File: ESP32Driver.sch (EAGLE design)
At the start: 90 parts, among them IC1 ESP-WROOM-32_VIA, IC3 FT231XQ, SW2 434111025826, T1.1 BC847A, T1.2 BC847A, T1.3 BC847A, T1.4 BC847A, X1 USB

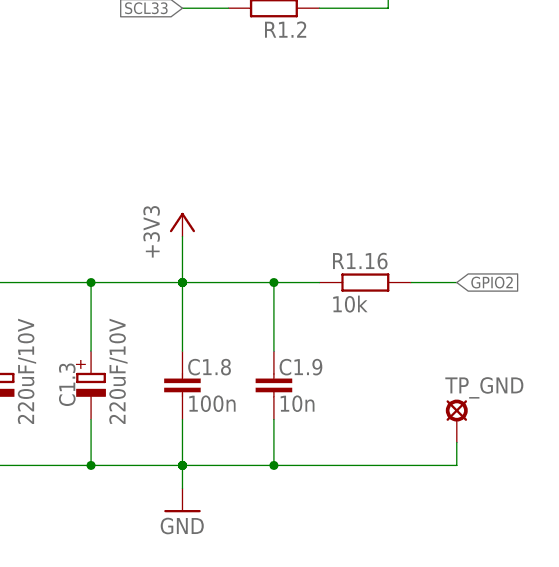
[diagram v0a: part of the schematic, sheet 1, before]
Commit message: delete GPIO2 pullup resistor
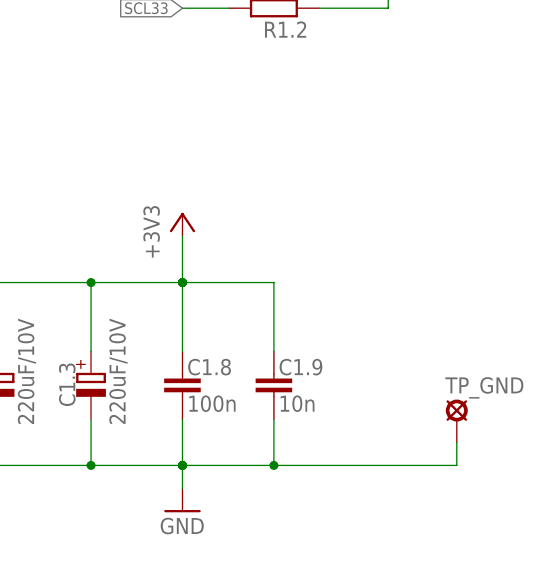
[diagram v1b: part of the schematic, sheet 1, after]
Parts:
- removed R1.16: 10k, rcl:R-EU_R0805
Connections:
- net +3V3: no longer R1.16.1
- net GPIO2: no longer R1.16.2
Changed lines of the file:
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@@
 <?xml version="1.0" encoding="utf-8"?>
 <!DOCTYPE eagle SYSTEM "eagle.dtd">
-<eagle version="9.4.0">
+<eagle version="9.6.2">
 <drawing>
 <settings>
@@
 <part name="GND19" library="supply1" deviceset="GND" device=""/>
 <part name="GND29" library="supply1" deviceset="GND" device=""/>
-<part name="R1.16" library="rcl" deviceset="R-EU_" device="R0805" value="10k"/>
 <part name="SW2" library="HW1_switches" deviceset="434111025826" device=""/>
 <part name="FRAME2" library="frames" library_urn="urn:adsk.eagle:library:229" deviceset="A4L-LOC" device=""/>
@@
 <attribute name="VALUE" x="71.12" y="68.58" size="1.778" layer="96"/>
 </instance>
-<instance part="R1.16" gate="G$1" x="226.06" y="58.42" smashed="yes">
-<attribute name="NAME" x="222.25" y="59.9186" size="1.778" layer="95"/>
-<attribute name="VALUE" x="222.25" y="55.118" size="1.778" layer="96"/>
-</instance>
 <instance part="SW2" gate="G$1" x="40.64" y="132.08" smashed="yes">
 <attribute name="NAME" x="36.83" y="130.175" size="1.778" layer="95" rot="R90"/>
@@
 <wire x1="205.74" y1="63.5" x2="205.74" y2="58.42" width="0.1524" layer="91"/>
 <junction x="205.74" y="58.42"/>
-<pinref part="R1.16" gate="G$1" pin="1"/>
-<wire x1="220.98" y1="58.42" x2="215.9" y2="58.42" width="0.1524" layer="91"/>
-<junction x="215.9" y="58.42"/>
 </segment>
 <segment>
@@
 </segment>
 <segment>
-<pinref part="R1.16" gate="G$1" pin="2"/>
-<wire x1="231.14" y1="58.42" x2="236.22" y2="58.42" width="0.1524" layer="91"/>
-<label x="236.22" y="58.42" size="1.27" layer="95" xref="yes"/>
-</segment>
-<segment>
